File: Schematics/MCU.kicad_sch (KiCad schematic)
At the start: 28 parts, among them J7 Microsemi_FlashPro-JTAG-10, U1 STM32F405RGTx, Y1 8mhz

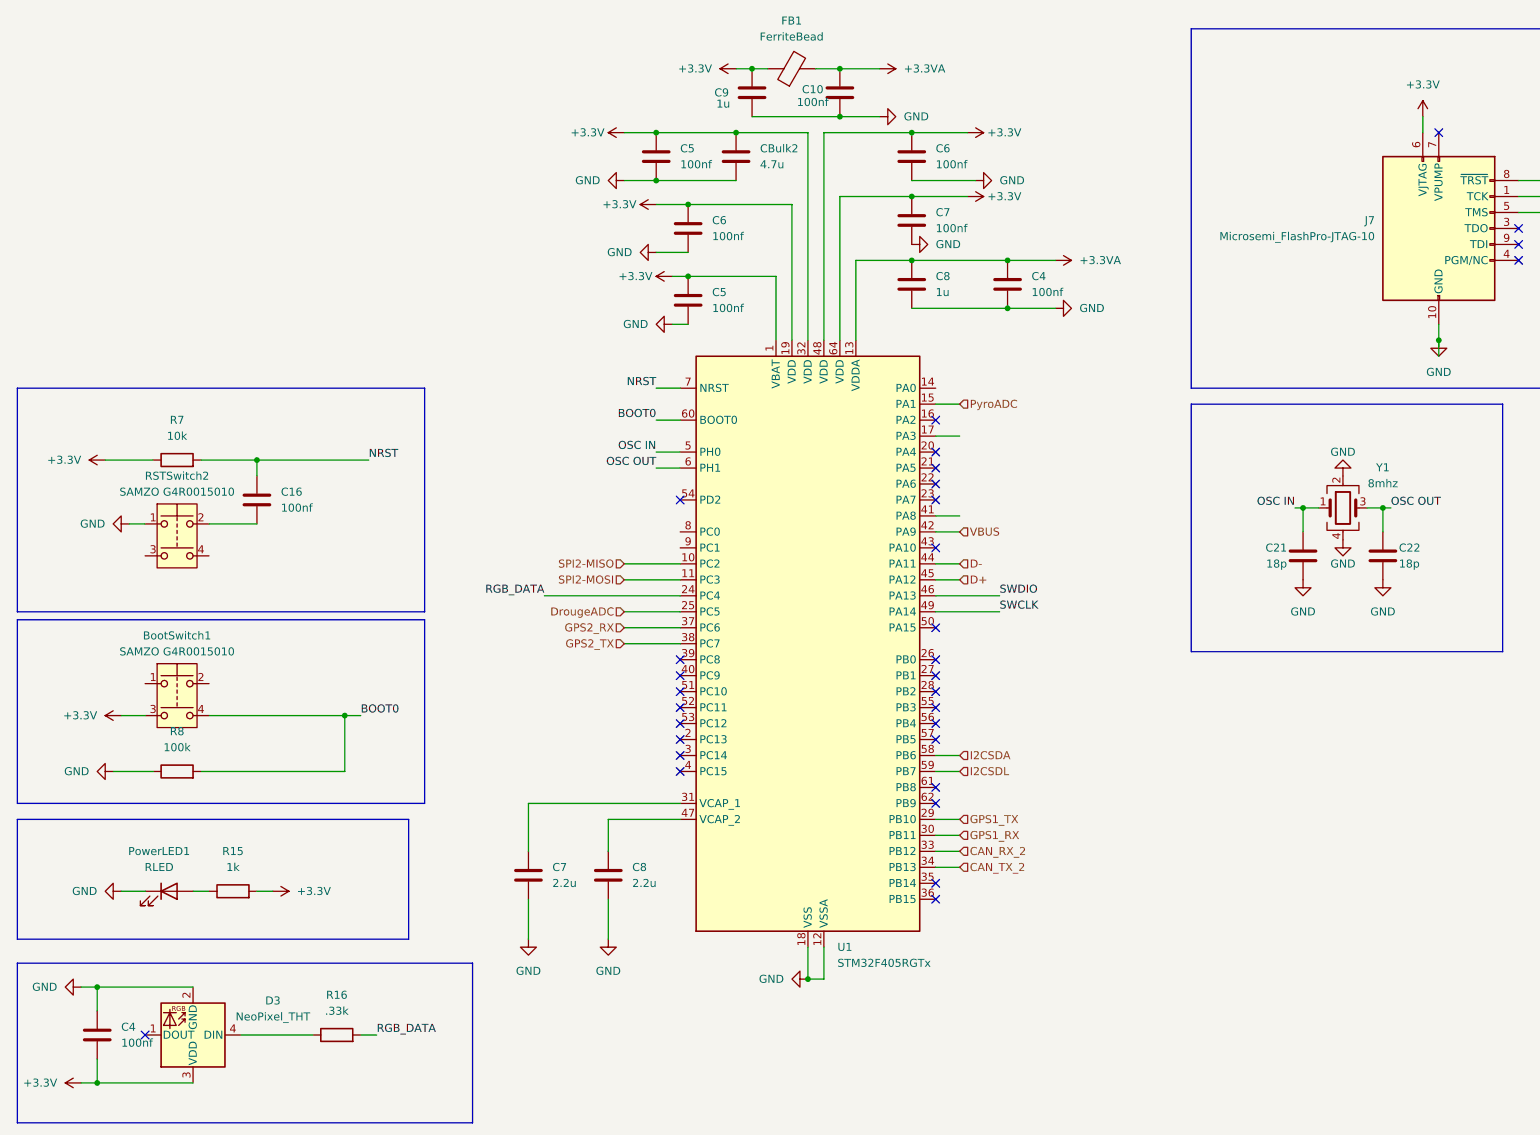
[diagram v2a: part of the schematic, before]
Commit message: added LCSC numbers and footprint values, need to connect schemeatic pins, then can start layout
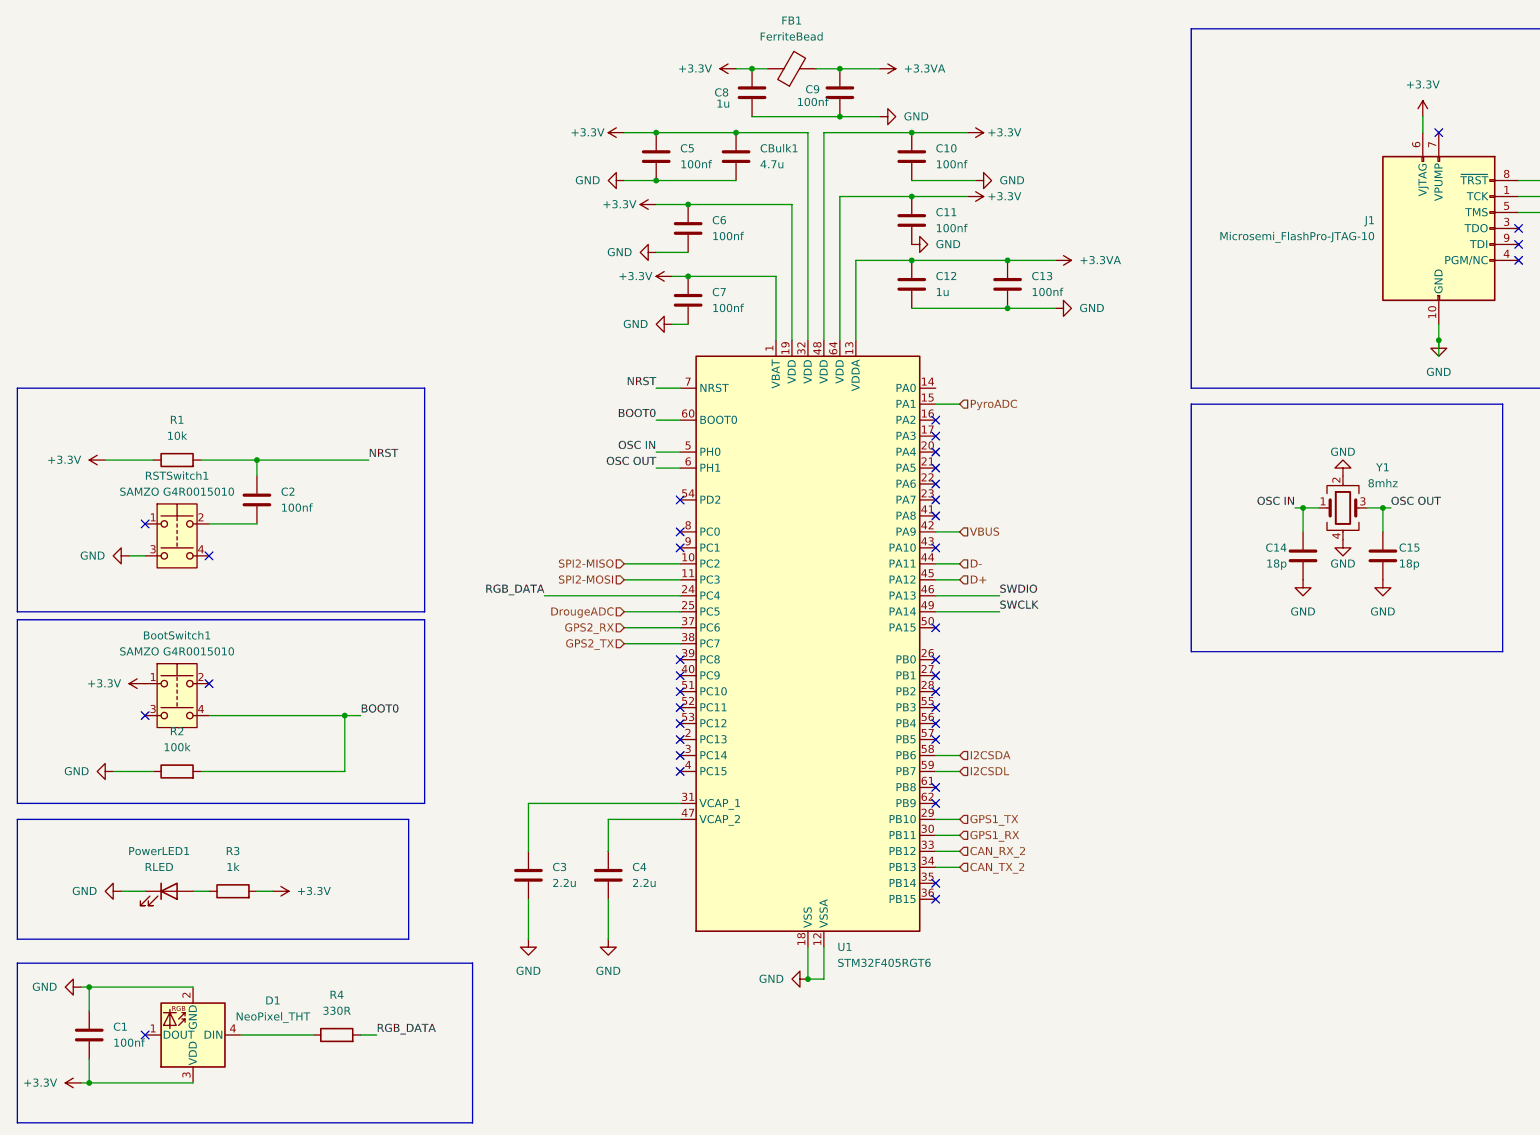
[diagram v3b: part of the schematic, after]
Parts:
- BootSwitch1: LCSC Part (none) -> C49393646
- C1: renamed from C4; footprint Resistor_SMD:R_0805_2012Metric_Pad1.20x1.40mm_HandSolder -> Capacitor_SMD:C_0805_2012Metric_Pad1.18x1.45mm_HandSolder; LCSC Part (none) -> C49678
- C10: renamed from C6; LCSC Part (none) -> C49678
- C11: renamed from C7; LCSC Part (none) -> C49678
- C12: renamed from C8; LCSC Part (none) -> C28323
- C13: renamed from C4; LCSC Part (none) -> C49678
- C2: renamed from C16; LCSC Part (none) -> C49678
- C3: renamed from C7; LCSC Part (none) -> C19110
- C4: renamed from C8; LCSC Part (none) -> C19110
- C5, C6: LCSC Part (none) -> C49678
- C7: renamed from C5; LCSC Part (none) -> C49678
- C8: renamed from C9; LCSC Part (none) -> C28323
- C9: renamed from C10; LCSC Part (none) -> C49678
- CBulk1: renamed from CBulk2; LCSC Part (none) -> C98192
- D1: renamed from D3; LCSC Part (none) -> C2827321
- FB1: LCSC Part (none) -> C85840
- J1: renamed from J7; LCSC Part (none) -> C585350
- PowerLED1: LCSC Part (none) -> C965799
- R1: renamed from R7; LCSC Part (none) -> C84376
- R2: renamed from R8; LCSC Part (none) -> C96346
- R3: renamed from R15; LCSC Part (none) -> C95781
- R4: renamed from R16; value .33k -> 330R; LCSC Part (none) -> C17630
- RSTSwitch1: renamed from RSTSwitch2; LCSC Part (none) -> C49393646
- U1: value STM32F405RGTx -> STM32F405RGT6; LCSC Part (none) -> C15742
- renumbered C21 to C14, C22 to C15
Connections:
- net +3.3V: now also BootSwitch1.1; no longer BootSwitch1.3
- net GND: now also RSTSwitch1.3; no longer RSTSwitch1.1
- no-connect marks 31 -> 39
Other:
- moved on the sheet: C1

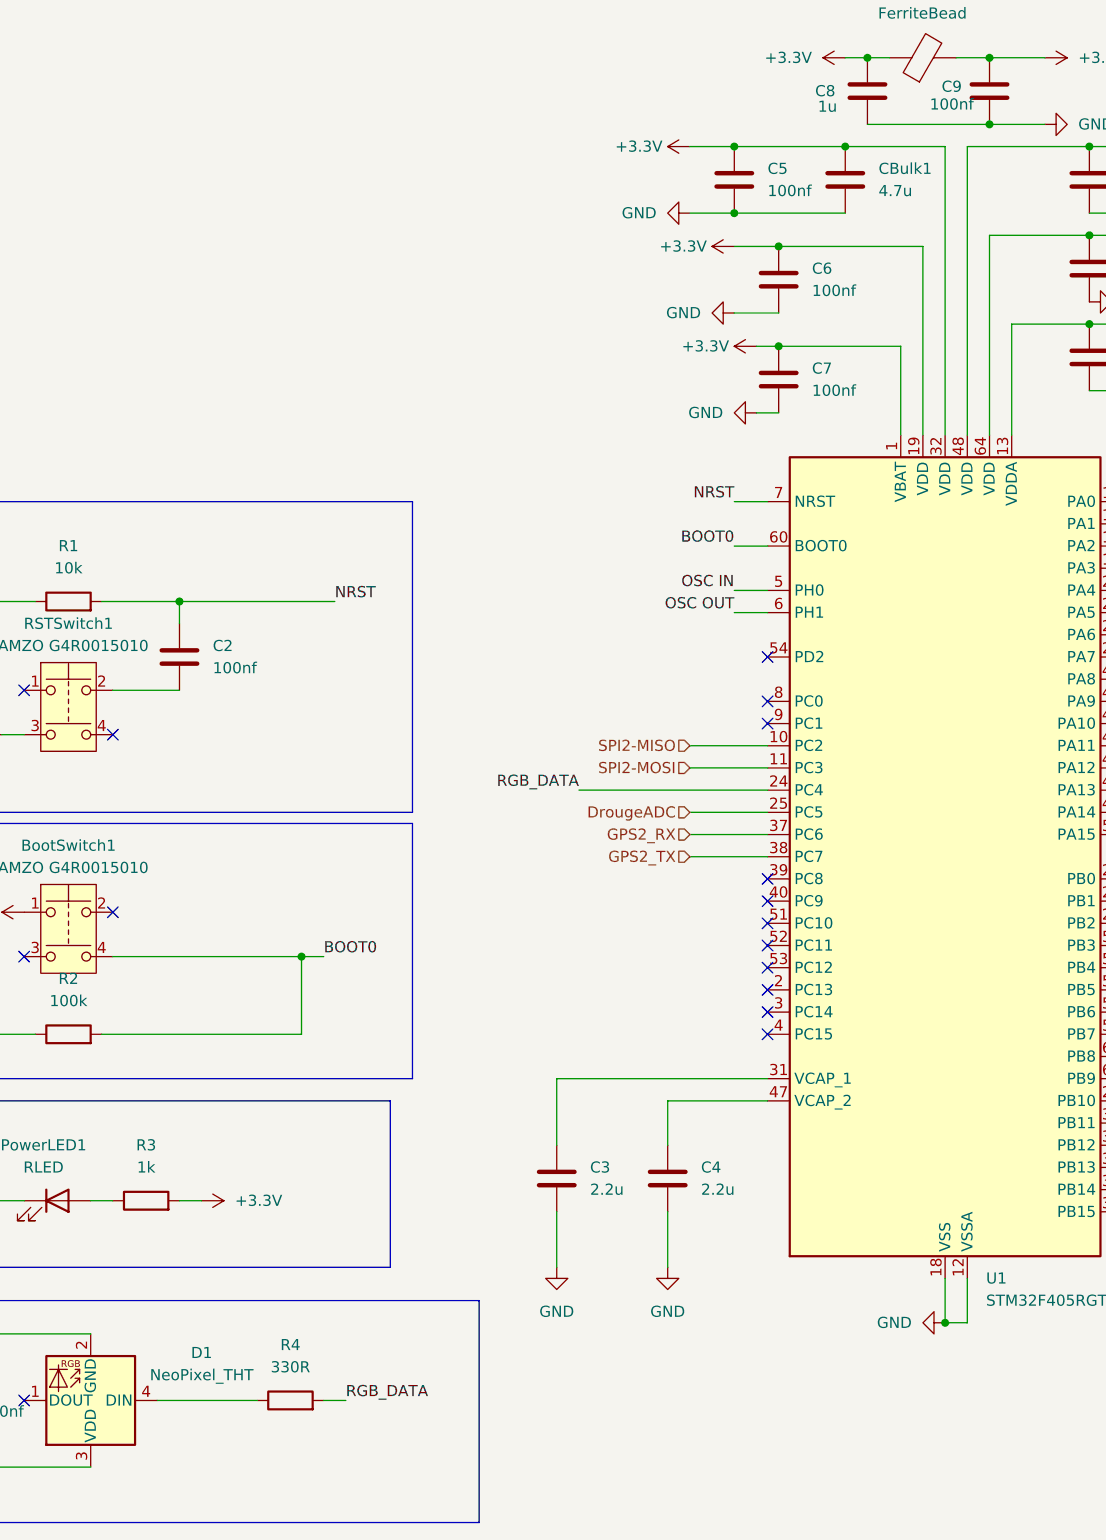
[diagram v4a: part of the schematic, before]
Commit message: fixed symbols and added diodes to power input before ldo
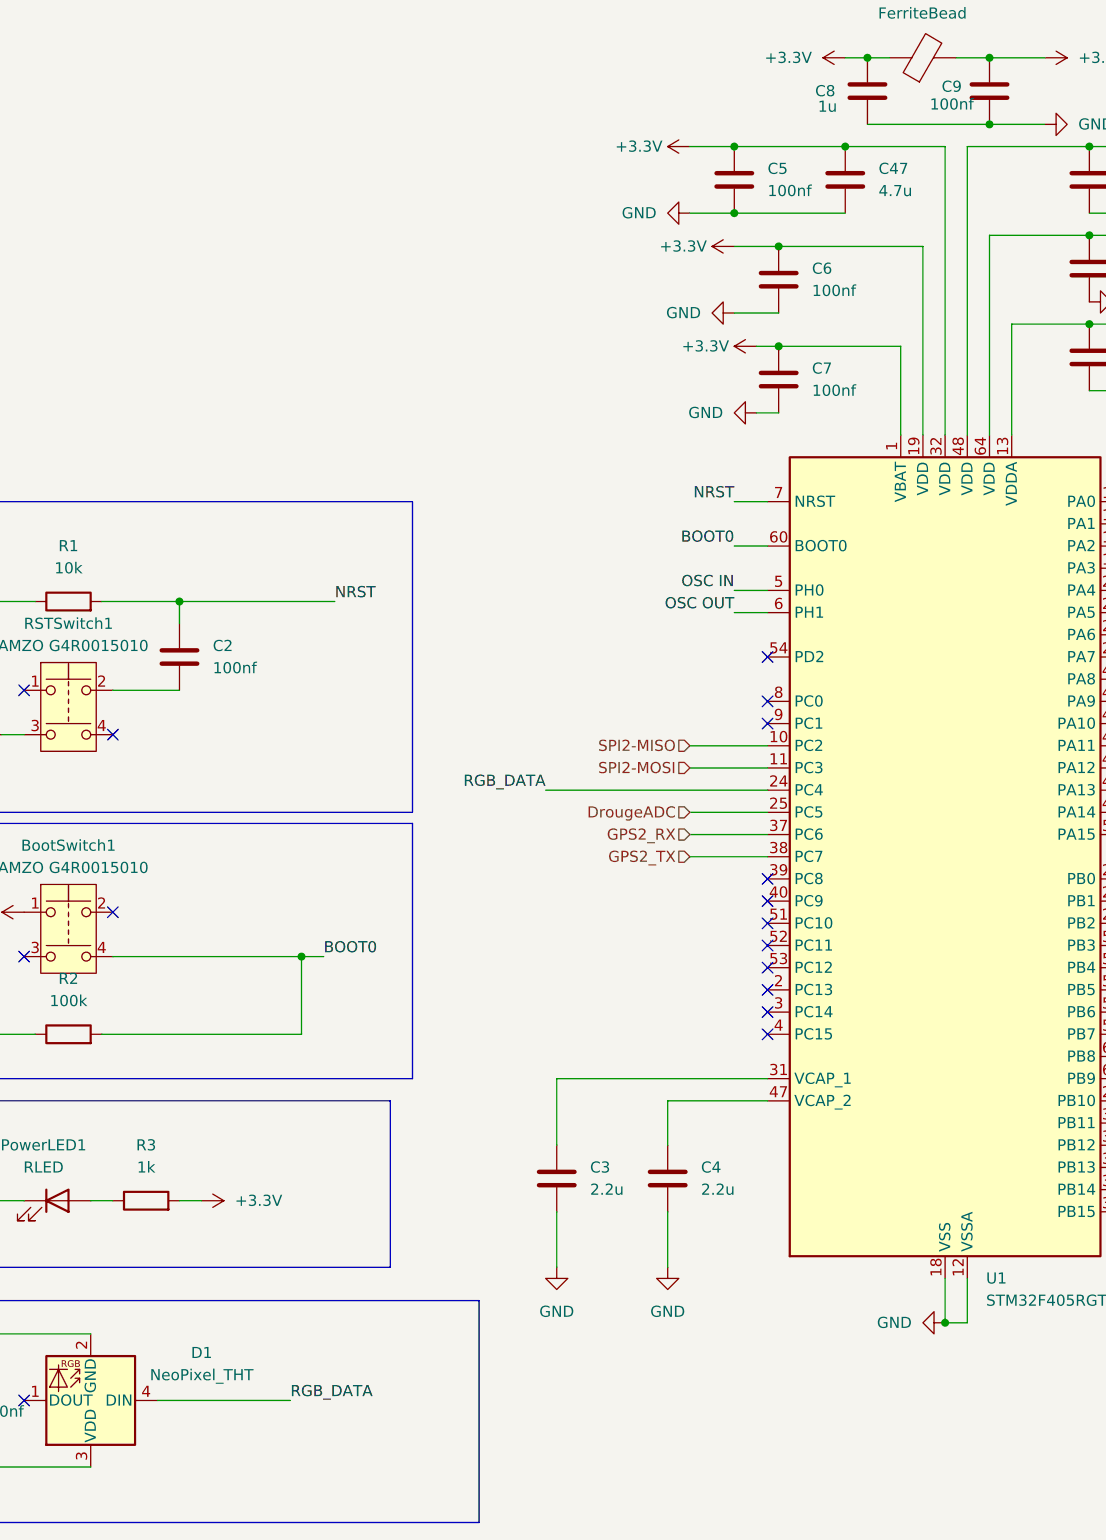
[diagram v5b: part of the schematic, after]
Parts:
- removed CBulk1: 4.7u, Capacitor_SMD:C_0805_2012Metric_Pad1.18x1.45mm_HandSolder, symbol Device:C
- removed R4: 330R, Resistor_SMD:R_0805_2012Metric_Pad1.20x1.40mm_HandSolder, symbol Device:R
- added C47: 4.7u, Capacitor_SMD:C_0805_2012Metric_Pad1.18x1.45mm_HandSolder, symbol Device:C
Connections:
- net +3.3V: now also C47.1
- net GND: now also C47.2
- net RGB_DATA: now also D1.4 (DIN)
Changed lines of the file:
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@@
 	)
 	(junction
-		(at 129.54 36.83)
+		(at 116.84 36.83)
 		(diameter 0)
 		(color 0 0 0 0)
 	)
 	(junction
-		(at 116.84 36.83)
+		(at 129.54 36.83)
 		(diameter 0)
 		(color 0 0 0 0)
@@
 	(wire
 		(pts
-			(xy 129.54 36.83) (xy 140.97 36.83)
-		)
-		(stroke
-			(width 0)
-			(type default)
-		)
-	)
-	(wire
-		(pts
 			(xy 148.59 57.15) (xy 148.59 69.85)
 		)
@@
 	(wire
 		(pts
-			(xy 50.8 180.34) (xy 62.23 180.34)
+			(xy 129.54 36.83) (xy 140.97 36.83)
+		)
+		(stroke
+			(width 0)
+			(type default)
+		)
+	)
+	(wire
+		(pts
+			(xy 50.8 180.34) (xy 66.04 180.34)
 		)
 		(stroke
@@
 	(wire
 		(pts
-			(xy 99.06 110.49) (xy 120.65 110.49)
+			(xy 95.25 110.49) (xy 120.65 110.49)
 		)
 		(stroke
@@
 	(wire
 		(pts
-			(xy 72.39 180.34) (xy 69.85 180.34)
-		)
-		(stroke
-			(width 0)
-			(type default)
-		)
-	)
-	(wire
-		(pts
 			(xy 67.31 129.54) (xy 69.85 129.54)
 		)
@@
 	)
 	(label "RGB_DATA"
-		(at 72.39 180.34 0)
+		(at 66.04 180.34 0)
 		(effects
 			(font
@@
 	)
 	(label "RGB_DATA"
-		(at 99.06 110.49 180)
+		(at 95.25 110.49 180)
 		(effects
 			(font
@@
 	)
 	(symbol
-		(lib_id "Device:R")
-		(at 66.04 180.34 90)
-		(unit 1)
-		(exclude_from_sim no)
-		(in_bom yes)
-		(on_board yes)
-		(dnp no)
-		(fields_autoplaced yes)
-		(property "Reference" "R4"
-			(at 66.04 173.99 90)
-			(effects
-				(font
-					(size 1.27 1.27)
-				)
-			)
-		)
-		(property "Value" "330R"
-			(at 66.04 176.53 90)
-			(effects
-				(font
-					(size 1.27 1.27)
-				)
-			)
-		)
-		(property "Footprint" "Resistor_SMD:R_0805_2012Metric_Pad1.20x1.40mm_HandSolder"
-			(at 66.04 182.118 90)
-			(effects
-				(font
-					(size 1.27 1.27)
-				)
-				(hide yes)
-			)
-		)
-		(property "Datasheet" "~"
-			(at 66.04 180.34 0)
-			(effects
-				(font
-					(size 1.27 1.27)
-				)
-				(hide yes)
-			)
-		)
-		(property "Description" "Resistor"
-			(at 66.04 180.34 0)
-			(effects
-				(font
-					(size 1.27 1.27)
-				)
-				(hide yes)
-			)
-		)
-		(property "LCSC Part" "C17630"
-			(at 66.04 180.34 90)
-			(effects
-				(font
-					(size 1.27 1.27)
-				)
-				(hide yes)
-			)
-		)
-		(pin "1"
-		)
-		(pin "2"
-		)
-		(instances
-			(project "flightcomputer2"
-				(path "/6cb3dda3-5fe8-4715-b831-354360aa3199/2415024d-c1fa-457e-8c6b-d01152b96a1d"
-					(reference "R4")
-					(unit 1)
-				)
-			)
-		)
-	)
-	(symbol
 		(lib_id "Device:Crystal_GND24")
 		(at 226.06 96.52 0)
@@
 	)
 	(symbol
-		(lib_id "Device:C")
-		(at 129.54 40.64 0)
-		(unit 1)
-		(exclude_from_sim no)
-		(in_bom yes)
-		(on_board yes)
-		(dnp no)
-		(fields_autoplaced yes)
-		(property "Reference" "CBulk1"
-			(at 133.35 39.3699 0)
-			(effects
-				(font
-					(size 1.27 1.27)
-				)
-				(justify left)
-			)
-		)
-		(property "Value" "4.7u"
-			(at 133.35 41.9099 0)
-			(effects
-				(font
-					(size 1.27 1.27)
-				)
-				(justify left)
-			)
-		)
-		(property "Footprint" "Capacitor_SMD:C_0805_2012Metric_Pad1.18x1.45mm_HandSolder"
-			(at 130.5052 44.45 0)
-			(effects
-				(font
-					(size 1.27 1.27)
-				)
-				(hide yes)
-			)
-		)
-		(property "Datasheet" "~"
-			(at 129.54 40.64 0)
-			(effects
-				(font
-					(size 1.27 1.27)
-				)
-				(hide yes)
-			)
-		)
-		(property "Description" "Unpolarized capacitor"
-			(at 129.54 40.64 0)
-			(effects
-				(font
-					(size 1.27 1.27)
-				)
-				(hide yes)
-			)
-		)
-		(property "LCSC Part" "C98192"
-			(at 129.54 40.64 0)
-			(effects
-				(font
-					(size 1.27 1.27)
-				)
-				(hide yes)
-			)
-		)
-		(pin "2"
-		)
-		(pin "1"
-		)
-		(instances
-			(project "flightcomputer2"
-				(path "/6cb3dda3-5fe8-4715-b831-354360aa3199/2415024d-c1fa-457e-8c6b-d01152b96a1d"
-					(reference "CBulk1")
-					(unit 1)
-				)
-			)
-		)
-	)
-	(symbol
 		(lib_id "power:+3.3V")
 		(at 166.37 36.83 270)
@@
 					(unit 1)
 				)
+			)
+		)
+	)
+	(symbol
+		(lib_id "Device:C")
+		(at 129.54 40.64 0)
+		(unit 1)
+		(exclude_from_sim no)
+		(in_bom yes)
+		(on_board yes)
+		(dnp no)
+		(fields_autoplaced yes)
+		(property "Reference" "C47"
+			(at 133.35 39.3699 0)
+			(effects
+				(font
+					(size 1.27 1.27)
+				)
+				(justify left)
+			)
+		)
+		(property "Value" "4.7u"
+			(at 133.35 41.9099 0)
+			(effects
+				(font
+					(size 1.27 1.27)
+				)
+				(justify left)
+			)
+		)
+		(property "Footprint" "Capacitor_SMD:C_0805_2012Metric_Pad1.18x1.45mm_HandSolder"
+			(at 130.5052 44.45 0)
+			(effects
+				(font
+					(size 1.27 1.27)
+				)
+				(hide yes)
+			)
+		)
+		(property "Datasheet" "~"
+			(at 129.54 40.64 0)
+			(effects
+				(font
+					(size 1.27 1.27)
+				)
+				(hide yes)
+			)
+		)
+		(property "Description" "Unpolarized capacitor"
+			(at 129.54 40.64 0)
+			(effects
+				(font
+					(size 1.27 1.27)
+				)
+				(hide yes)
+			)
+		)
+		(property "LCSC Part" "C98192"
+			(at 129.54 40.64 0)
+			(effects
+				(font
+					(size 1.27 1.27)
+				)
+				(hide yes)
+			)
+		)
+		(pin "1"
+		)
+		(pin "2"
+		)
+		(instances
+			(project "flightcomputer2"
+				(path "/6cb3dda3-5fe8-4715-b831-354360aa3199/2415024d-c1fa-457e-8c6b-d01152b96a1d"
+					(reference "C47")
+					(unit 1)
+				)
